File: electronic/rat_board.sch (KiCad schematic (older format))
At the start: 52 parts, among them P1 FRONT_LEFT_IR, P2 SIDE_LEFT_IR, P3 SIDE_RIGHT_IR, P4 FRONT_RIGHT_IR, P5 LEFT_MOTOR, P6 RIGHT_MOTOR, P7 JTAG, P8 CONN_01X02, SW1 SW_PUSH_SMALL_H, SW2 SWITCH_INV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

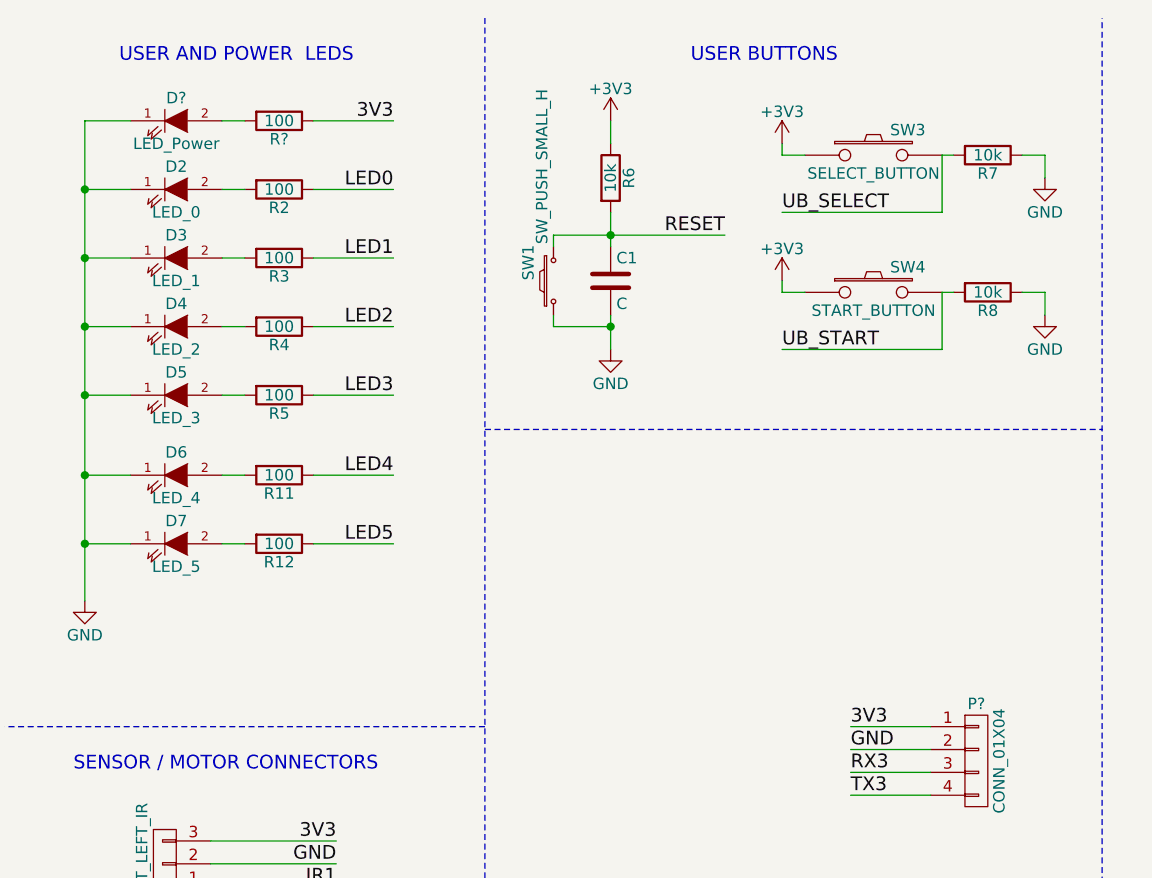
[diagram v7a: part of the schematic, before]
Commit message: component values on board
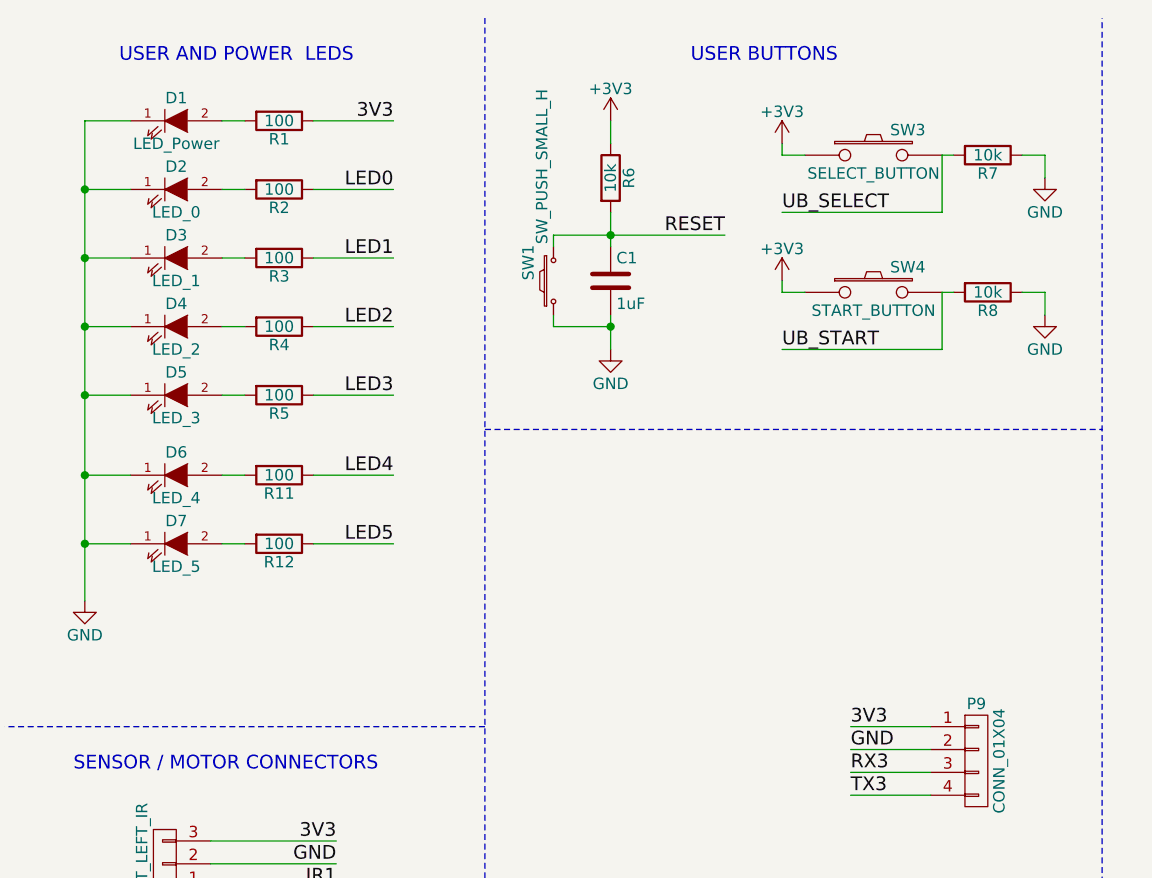
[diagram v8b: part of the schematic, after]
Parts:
- C1: value C -> 1uF
- D1: renamed from D?; footprint LEDs:LED-3MM -> LEDs:LED_0603
- gave numbers to parts that had none: 2
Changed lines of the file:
@@
 P 3150 1650
 F 0 "C1" H 3175 1750 50  0000 L CNN
-F 1 "C" H 3175 1550 50  0000 L CNN
+F 1 "1uF" H 3175 1550 50  0000 L CNN
 F 2 "Capacitors_SMD:C_0603_HandSoldering" H 3188 1500 50  0001 C CNN
 F 3 "" H 3150 1650 50  0000 C CNN
@@
 NoConn ~ 5650 3100
 $Comp
-L CONN_01X04 P?
+L CONN_01X04 P9
 U 1 1 58938DC7
 P 4750 3750
-F 0 "P?" H 4750 4000 50  0000 C CNN
+F 0 "P9" H 4750 4000 50  0000 C CNN
 F 1 "CONN_01X04" V 4850 3750 50  0000 C CNN
-F 2 "" H 4750 3750 50  0000 C CNN
+F 2 "" H 4750 3750 50  0001 C CNN
 F 3 "" H 4750 3750 50  0000 C CNN
 	1    4750 3750
@@
 	4200 3900 4550 3900
 $Comp
-L LED D?
+L LED D1
 U 1 1 589F2FBF
 P 1250 950
-F 0 "D?" H 1250 1050 50  0000 C CNN
+F 0 "D1" H 1250 1050 50  0000 C CNN
 F 1 "LED_Power" H 1250 850 50  0000 C CNN
-F 2 "LEDs:LED-3MM" H 1250 950 50  0001 C CNN
+F 2 "LEDs:LED_0603" H 1250 950 50  0001 C CNN
 F 3 "" H 1250 950 50  0000 C CNN
 	1    1250 950
@@
 $EndComp
 $Comp
-L R R?
+L R R1
 U 1 1 589F2FC5
 P 1700 950
-F 0 "R?" V 1780 950 50  0000 C CNN
+F 0 "R1" V 1780 950 50  0000 C CNN
 F 1 "100" V 1700 950 50  0000 C CNN
 F 2 "Resistors_SMD:R_0603_HandSoldering" V 1630 950 50  0001 C CNN
